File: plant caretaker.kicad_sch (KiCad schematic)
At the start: 1 part, among them U4 ESP32-C3

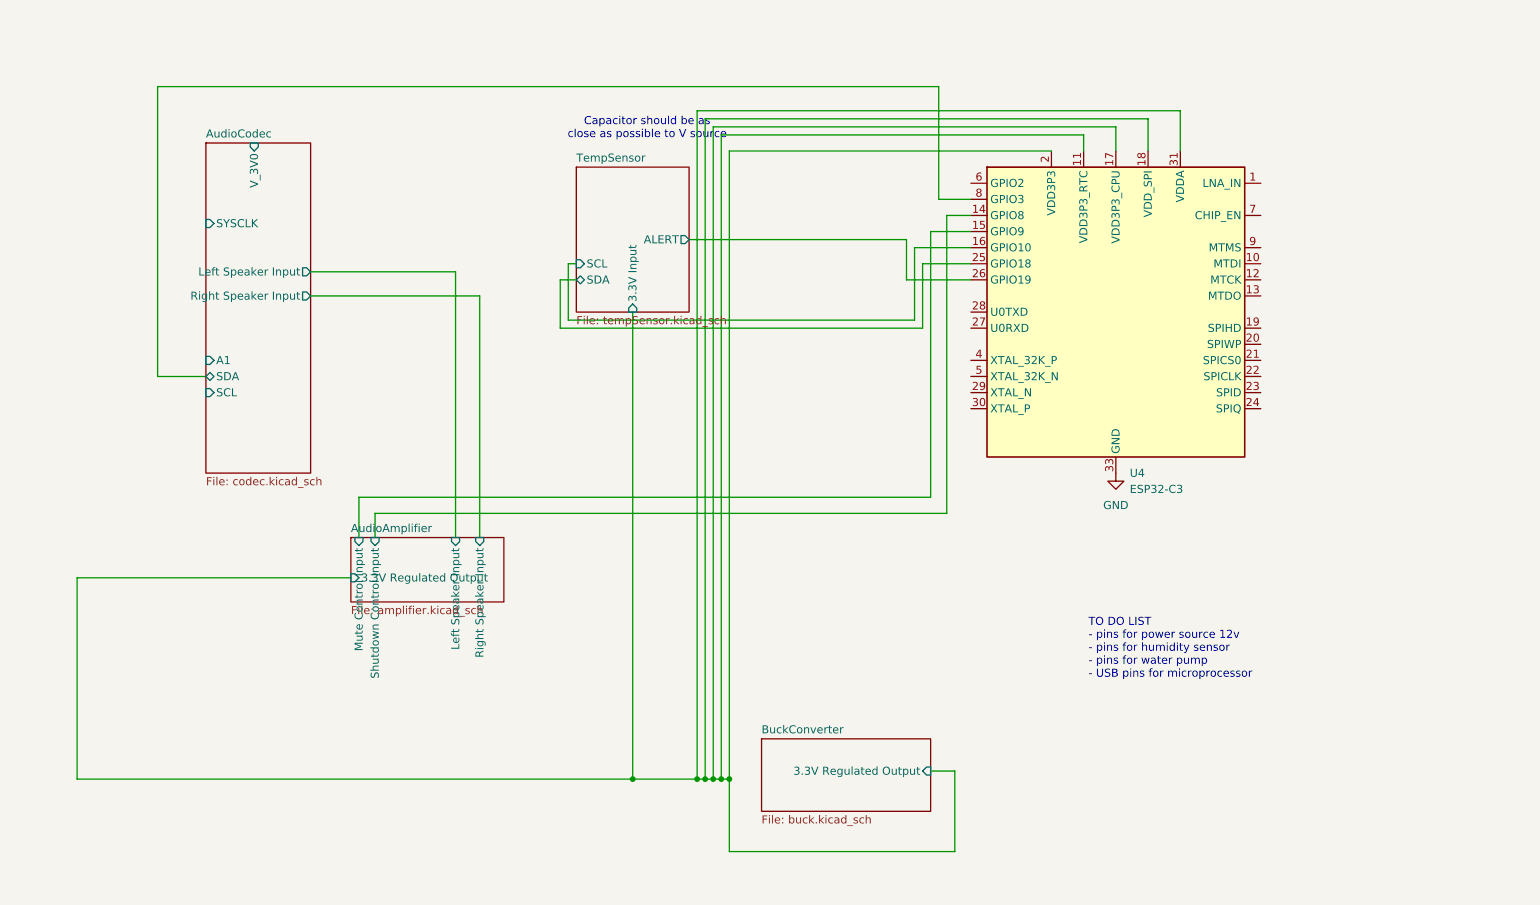
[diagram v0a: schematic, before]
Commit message: Fixed connections and digital output of codec
Used NC instead of GND for output pins
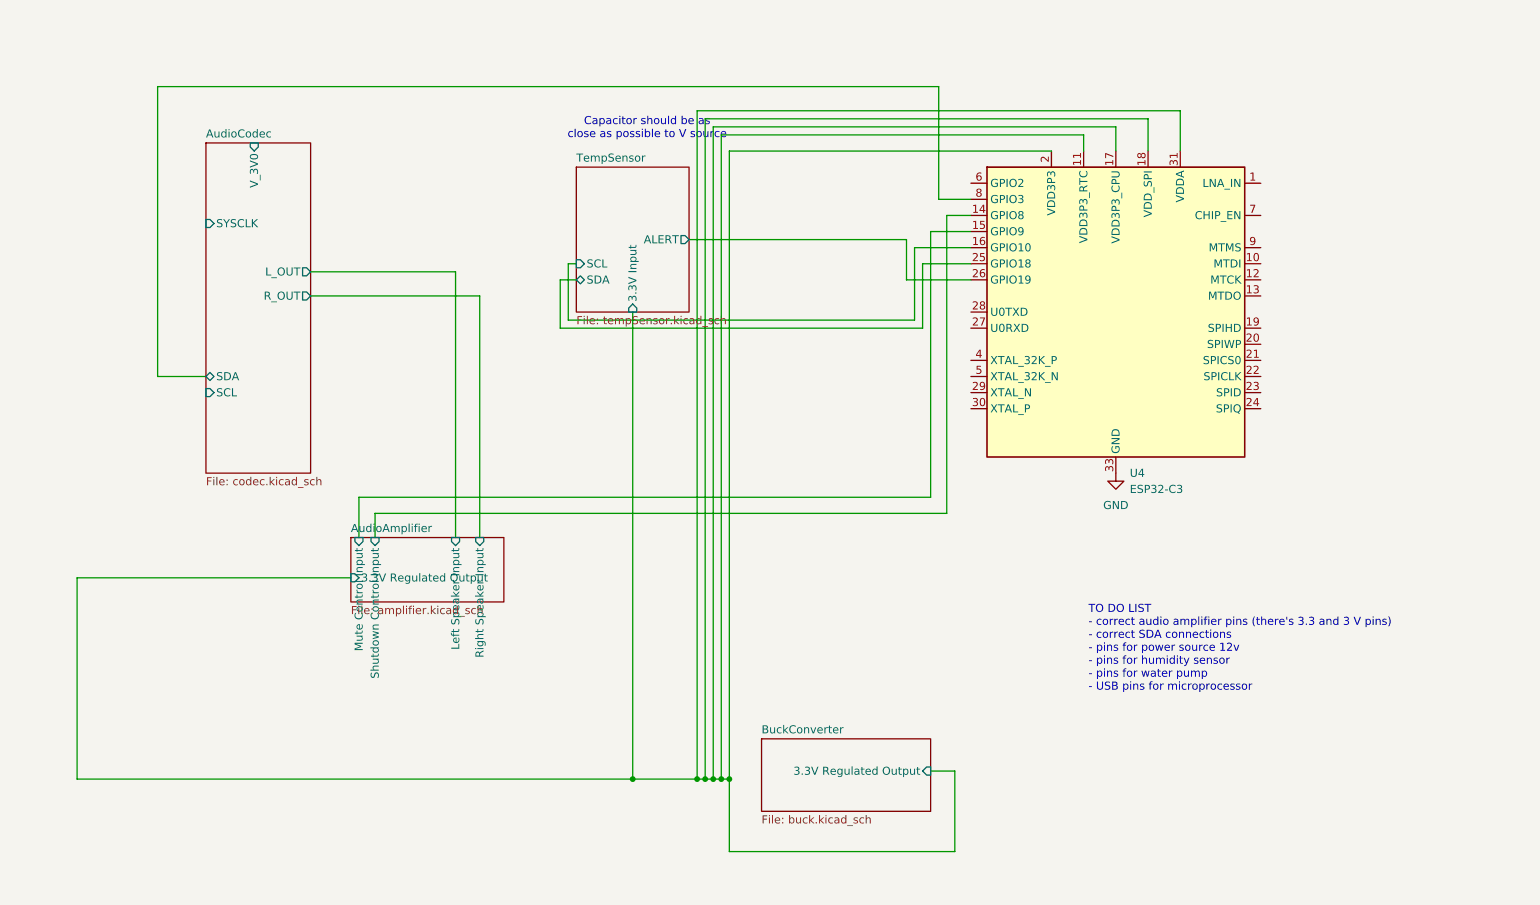
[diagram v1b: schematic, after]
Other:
- sheet AudioCodec ports: added L_OUT, R_OUT; removed A1, Left Speaker Input, Right Speaker Input
- note added: "TO DO LIST - correct audio amplifier pins (there's 3.3 and 3 V pins) - correct SDA connections - pins for power source 12v - pins for humidity sensor - pins for water pump - USB pins for microprocessor"
- note removed: "TO DO LIST - pins for power source 12v - pins for humidity sensor - pins for water pump - USB pins for microprocessor"
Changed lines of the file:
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@@
 		)
 	)
-	(text "TO DO LIST\n- pins for power source 12v\n- pins for humidity sensor\n- pins for water pump\n- USB pins for microprocessor"
+	(text "TO DO LIST\n- correct audio amplifier pins (there's 3.3 and 3 V pins)\n- correct SDA connections\n- pins for power source 12v\n- pins for humidity sensor\n- pins for water pump\n- USB pins for microprocessor"
 		(exclude_from_sim no)
 		(at 223.012 115.316 0)
@@
 			)
 		)
-		(pin "A1" input
-			(at 83.82 69.85 180)
-			(effects
-				(font
-					(size 1.27 1.27)
-				)
-				(justify left)
-			)
-		)
 		(pin "SCL" input
 			(at 83.82 74.93 180)
@@
 			)
 		)
-		(pin "Right Speaker Input" output
-			(at 100.33 59.69 0)
-			(effects
-				(font
-					(size 1.27 1.27)
-				)
-				(justify right)
-			)
-		)
-		(pin "Left Speaker Input" output
-			(at 100.33 55.88 0)
-			(effects
-				(font
-					(size 1.27 1.27)
-				)
-				(justify right)
-			)
-		)
 		(pin "V_3V0" input
 			(at 91.44 35.56 90)
 			(effects
 				(font
+					(size 1.27 1.27)
+				)
+				(justify right)
+			)
+		)
+		(pin "R_OUT" output
+			(at 100.33 59.69 0)
+			(effects
+				(font
+					(size 1.27 1.27)
+				)
+				(justify right)
+			)
+		)
+		(pin "L_OUT" output
+			(at 100.33 55.88 0)
+			(effects
+				(font

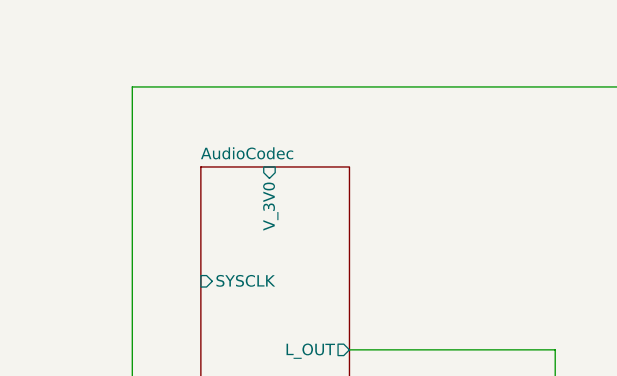
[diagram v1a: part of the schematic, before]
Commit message: Added voltage source for testing to main
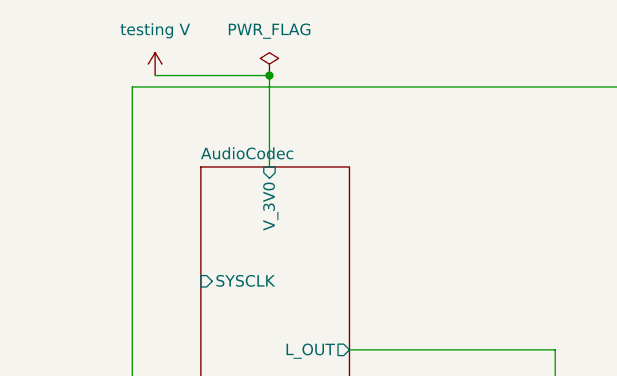
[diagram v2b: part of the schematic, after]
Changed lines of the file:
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@@
+	)
+	(junction
+		(at 91.44 25.4)
+		(diameter 0)
+		(color 0 0 0 0)
 	)
 	(junction
@@
 		(pts
 			(xy 195.58 63.5) (xy 195.58 52.07)
+		)
+		(stroke
+			(width 0)
+			(type default)
+		)
+	)
+	(wire
+		(pts
+			(xy 78.74 25.4) (xy 91.44 25.4)
+		)
+		(stroke
+			(width 0)
+			(type default)
+		)
+	)
+	(wire
+		(pts
+			(xy 91.44 25.4) (xy 91.44 35.56)
 		)
 		(stroke
@@
 			(font
 				(size 1.27 1.27)
+			)
+		)
+	)
+	(symbol
+		(lib_id "power:PWR_FLAG")
+		(at 91.44 25.4 0)
+		(unit 1)
+		(exclude_from_sim no)
+		(in_bom yes)
+		(on_board yes)
+		(dnp no)
+		(fields_autoplaced yes)
+		(property "Reference" "#FLG08"
+			(at 91.44 23.495 0)
+			(effects
+				(font
+					(size 1.27 1.27)
+				)
+				(hide yes)
+			)
+		)
+		(property "Value" "PWR_FLAG"
+			(at 91.44 20.32 0)
+			(effects
+				(font
+					(size 1.27 1.27)
+				)
+			)
+		)
+		(property "Footprint" ""
+			(at 91.44 25.4 0)
+			(effects
+				(font
+					(size 1.27 1.27)
+				)
+				(hide yes)
+			)
+		)
+		(property "Datasheet" "~"
+			(at 91.44 25.4 0)
+			(effects
+				(font
+					(size 1.27 1.27)
+				)
+				(hide yes)
+			)
+		)
+		(property "Description" "Special symbol for telling ERC where power comes from"
+			(at 91.44 25.4 0)
+			(effects
+				(font
+					(size 1.27 1.27)
+				)
+				(hide yes)
+			)
+		)
+		(pin "1"
+		)
+		(instances
+			(project "plant caretaker"
+				(path "/23b35dcc-615e-4aec-abee-c26cc3d8b906"
+					(reference "#FLG08")
+					(unit 1)
+				)
 			)
 		)
@@
 					(unit 1)
 				)
+			)
+		)
+	)
+	(symbol
+		(lib_id "power:+3V0")
+		(at 78.74 25.4 0)
+		(unit 1)
+		(exclude_from_sim no)
+		(in_bom yes)
+		(on_board yes)
+		(dnp no)
+		(fields_autoplaced yes)
+		(property "Reference" "#PWR019"
+			(at 78.74 29.21 0)
+			(effects
+				(font
+					(size 1.27 1.27)
+				)
+				(hide yes)
+			)
+		)
+		(property "Value" "testing V"
+			(at 78.74 20.32 0)
+			(effects
+				(font
+					(size 1.27 1.27)
+				)
+			)
+		)
+		(property "Footprint" ""
+			(at 78.74 25.4 0)
+			(effects
+				(font
+					(size 1.27 1.27)
+				)
+				(hide yes)
+			)
+		)
+		(property "Datasheet" ""
+			(at 78.74 25.4 0)
+			(effects
+				(font
+					(size 1.27 1.27)
+				)
+				(hide yes)
+			)
+		)
+		(property "Description" "Power symbol creates a global label with name \"+3V0\""
+			(at 78.74 25.4 0)
+			(effects
+				(font
+					(size 1.27 1.27)
+				)
+				(hide yes)
+			)
+		)
+		(pin "1"
+		)
+		(instances
+			(project ""
+				(path "/23b35dcc-615e-4aec-abee-c26cc3d8b906"
+					(reference "#PWR019")
+					(unit 1)
+				)

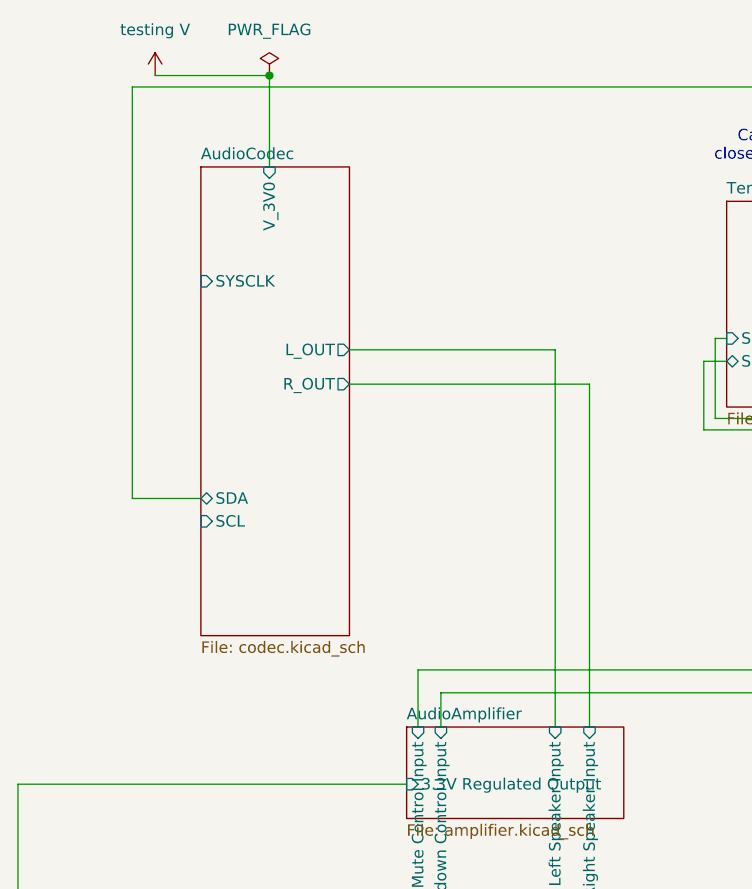
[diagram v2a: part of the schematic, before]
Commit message: Codec finished and added notes
Corrected input and ouput pins, added NOTES file and cleaned up
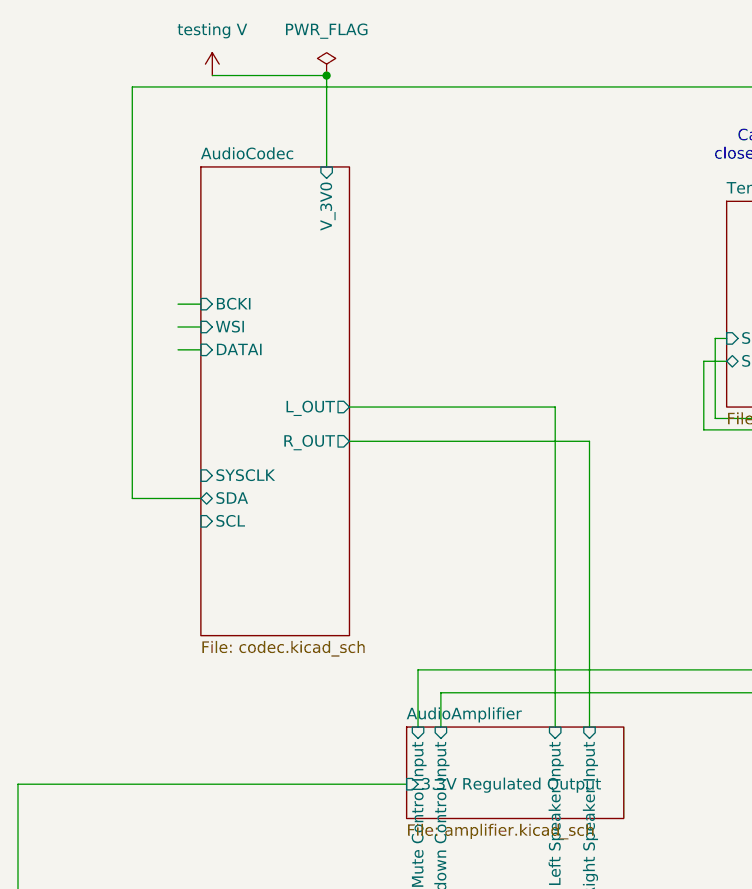
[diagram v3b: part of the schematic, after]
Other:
- sheet AudioCodec ports: added BCKI, DATAI, WSI; removed none
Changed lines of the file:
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@@
 	)
 	(junction
-		(at 91.44 25.4)
+		(at 97.79 25.4)
 		(diameter 0)
 		(color 0 0 0 0)
@@
 	(wire
 		(pts
-			(xy 100.33 59.69) (xy 127 59.69)
+			(xy 100.33 66.04) (xy 127 66.04)
 		)
 		(stroke
@@
 	(wire
 		(pts
+			(xy 81.28 55.88) (xy 83.82 55.88)
+		)
+		(stroke
+			(width 0)
+			(type default)
+		)
+	)
+	(wire
+		(pts
 			(xy 195.58 52.07) (xy 204.47 52.07)
 		)
@@
 	(wire
 		(pts
+			(xy 81.28 53.34) (xy 83.82 53.34)
+		)
+		(stroke
+			(width 0)
+			(type default)
+		)
+	)
+	(wire
+		(pts
 			(xy 163.83 33.02) (xy 163.83 135.89)
 		)
@@
 	(wire
 		(pts
-			(xy 100.33 55.88) (xy 123.19 55.88)
+			(xy 100.33 62.23) (xy 123.19 62.23)
 		)
 		(stroke
@@
 	(wire
 		(pts
-			(xy 123.19 55.88) (xy 123.19 97.79)
+			(xy 123.19 62.23) (xy 123.19 97.79)
 		)
 		(stroke
@@
 	(wire
 		(pts
-			(xy 127 59.69) (xy 127 97.79)
+			(xy 127 66.04) (xy 127 97.79)
 		)
 		(stroke
@@
 	(wire
 		(pts
+			(xy 97.79 25.4) (xy 97.79 35.56)
+		)
+		(stroke
+			(width 0)
+			(type default)
+		)
+	)
+	(wire
+		(pts
 			(xy 198.12 91.44) (xy 198.12 49.53)
 		)
@@
 	(wire
 		(pts
-			(xy 78.74 25.4) (xy 91.44 25.4)
-		)
-		(stroke
-			(width 0)
-			(type default)
-		)
-	)
-	(wire
-		(pts
-			(xy 91.44 25.4) (xy 91.44 35.56)
+			(xy 85.09 25.4) (xy 97.79 25.4)
 		)
 		(stroke
@@
 		(pts
 			(xy 110.49 93.98) (xy 200.66 93.98)
+		)
+		(stroke
+			(width 0)
+			(type default)
+		)
+	)
+	(wire
+		(pts
+			(xy 81.28 50.8) (xy 83.82 50.8)
 		)
 		(stroke
@@
 	(symbol
 		(lib_id "power:PWR_FLAG")
-		(at 91.44 25.4 0)
+		(at 97.79 25.4 0)
 		(unit 1)
 		(exclude_from_sim no)
@@
 		(fields_autoplaced yes)
 		(property "Reference" "#FLG08"
-			(at 91.44 23.495 0)
+			(at 97.79 23.495 0)
 			(effects
 				(font
@@
 		)
 		(property "Value" "PWR_FLAG"
-			(at 91.44 20.32 0)
+			(at 97.79 20.32 0)
 			(effects
 				(font
@@
 		)
 		(property "Footprint" ""
-			(at 91.44 25.4 0)
+			(at 97.79 25.4 0)
 			(effects
 				(font
@@
 		)
 		(property "Datasheet" "~"
-			(at 91.44 25.4 0)
+			(at 97.79 25.4 0)
 			(effects
 				(font
@@
 		)
 		(property "Description" "Special symbol for telling ERC where power comes from"
-			(at 91.44 25.4 0)
+			(at 97.79 25.4 0)
 			(effects
 				(font
@@
 	(symbol
 		(lib_id "power:+3V0")
-		(at 78.74 25.4 0)
+		(at 85.09 25.4 0)
 		(unit 1)
 		(exclude_from_sim no)
@@
 		(fields_autoplaced yes)
 		(property "Reference" "#PWR019"
-			(at 78.74 29.21 0)
+			(at 85.09 29.21 0)
 			(effects
 				(font
@@
 		)
 		(property "Value" "testing V"
-			(at 78.74 20.32 0)
+			(at 85.09 20.32 0)
 			(effects
 				(font
@@
 		)
 		(property "Footprint" ""
-			(at 78.74 25.4 0)
+			(at 85.09 25.4 0)
 			(effects
 				(font
@@
 		)
 		(property "Datasheet" ""
-			(at 78.74 25.4 0)
+			(at 85.09 25.4 0)
 			(effects
 				(font
@@
 		)
 		(property "Description" "Power symbol creates a global label with name \"+3V0\""
-			(at 78.74 25.4 0)
+			(at 85.09 25.4 0)
 			(effects
 				(font
@@
 		)
 		(pin "SYSCLK" input
-			(at 83.82 48.26 180)
+			(at 83.82 69.85 180)
 			(effects
 				(font
@@
 		)
 		(pin "V_3V0" input
-			(at 91.44 35.56 90)
+			(at 97.79 35.56 90)
 			(effects
 				(font
@@
 		)
 		(pin "R_OUT" output
-			(at 100.33 59.69 0)
+			(at 100.33 66.04 0)
 			(effects
 				(font
@@
 		)
 		(pin "L_OUT" output
-			(at 100.33 55.88 0)
+			(at 100.33 62.23 0)
 			(effects
 				(font
@@
 			)
 		)
+		(pin "WSI" input
+			(at 83.82 53.34 180)
+			(effects
+				(font
+					(size 1.27 1.27)
+				)
+				(justify left)
+			)
+		)
+		(pin "DATAI" input
+			(at 83.82 55.88 180)
+			(effects
+				(font
+					(size 1.27 1.27)
+				)
+				(justify left)
+			)
+		)
+		(pin "BCKI" input
+			(at 83.82 50.8 180)
+			(effects
+				(font
+					(size 1.27 1.27)
+				)
+				(justify left)
+			)
+		)

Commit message: Cleanup, sorting, adding external parts
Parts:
- added J1: USB3_A, symbol Connector:USB3_A
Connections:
- net TempSensor/SCL is gone; now on net AudioCodec/SCL: U4.16 (GPIO10)
- net AudioAmplifier/3.3V Regulated Output renamed AudioAmplifier/3.3V_IN
- net AudioAmplifier/Mute Control Input renamed AudioAmplifier/MUTE_IN
- net AudioAmplifier/Shutdown Control Input: no longer names the net of U4.14 (GPIO8)
- net TempSensor/SDA renamed AudioAmplifier/SHDN_IN
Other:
- sheet AudioAmplifier ports: added 3.3V_IN, L_IN, MUTE_IN, R_IN, SHDN_IN; removed 3.3V Regulated Output, Left Speaker Input, Mute Control Input, Right Speaker Input, Shutdown Control Input
- sheet TempSensor ports: added 3.3V_IN; removed 3.3V Input
- note added: "TO DO LIST - pins for power source 12v - pins for humidity sensor - pins for water pump - USB pins for microprocessor"
- note removed: "TO DO LIST - correct audio amplifier pins (there's 3.3 and 3 V pins) - correct SDA connections - pins for power source 12v - pins for humidity sensor - pins for water pump - USB pins for microprocessor"

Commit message: Globglobgabgalab
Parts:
- removed J1: USB3_A, symbol Connector:USB3_A
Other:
- moved on the sheet: U4
